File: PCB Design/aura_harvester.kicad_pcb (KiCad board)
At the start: 2 copper layers, 44.9 x 21.1 mm, 34 parts, among them J1 Conn_01x01_Pin, J2 Conn_01x01_Pin, J3 Conn_01x01_Pin, J4 Conn_01x01_Pin, J5 Conn_01x01_Pin, U1 ADG936BRUZ

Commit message: AURA PCB design
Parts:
- moved C11 70.6 mm to (64.2, 51.8), turned to 90 degrees
- moved L1 68.2 mm to (70.5, 49.6), turned to 180 degrees
- moved C8 62.0 mm to (69.0, 55.2), turned to -90 degrees
- moved C7 60.0 mm to (69.4, 61.8), turned to -90 degrees
- moved C3 55.0 mm to (72.5, 55.2), turned to -90 degrees
- moved C6 53.4 mm to (78.3, 55.1), turned to -90 degrees
- moved C1 52.5 mm to (72.2, 61.8), turned to -90 degrees
- moved R2 51.6 mm to (82.9, 63.8), turned to 180 degrees
- moved C2 51.5 mm to (75.2, 55.2), turned to -90 degrees
- moved C4 51.4 mm to (75.1, 61.7), turned to -90 degrees
- moved J1 50.3 mm to (64.2, 47.8)
- moved C5 49.5 mm to (78.2, 61.6), turned to -90 degrees
- moved C10 43.9 mm to (88.2, 60.6), turned to -90 degrees
- moved D1 43.7 mm to (68.2, 58.5), turned to -90 degrees
- moved D2 42.8 mm to (69.7, 58.5), turned to 90 degrees
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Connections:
- C10 pad 2: Net-(C10-Pad2) -> GND
- C9 pad 2: Net-(C10-Pad2) -> GND
- R2 pad 2: Net-(R2-Pad2) -> GND
- U1 pad 11: Net-(R2-Pad2) -> GND
- U1 pad 13: Net-(R2-Pad2) -> GND
- U1 pad 15: Net-(R2-Pad2) -> GND
- U1 pad 16: Net-(R2-Pad2) -> GND
- U1 pad 18: Net-(U1-GND-Pad18) -> GND
- U1 pad 20: Net-(U1-GND-Pad18) -> GND
- U1 pad 3: Net-(C10-Pad2) -> GND
- U1 pad 5: Net-(C10-Pad2) -> GND
- U1 pad 6: Net-(C10-Pad2) -> GND
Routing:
- net /CLK: track 0.00 -> 5.64 mm
- added copper zone on F.Cu, net +3V3
- added copper zone on F.Cu, net /M_IN
- added copper zone on F.Cu, net Net-(D1-A)
- added copper zone on F.Cu, net Net-(D3-A)
- added copper zone on F.Cu, net Net-(D5-A)
- added copper zone on F.Cu, net Net-(D8-A)
- added copper zone on F.Cu, net Net-(U1-RF2A)
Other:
- board size 44.9 x 21.1 mm -> 34.3 x 21.1 mm

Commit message: Completed Routing and Silkscreen
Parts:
- added G***: LOGO, Logos:Lions_logo, F.Cu at (60.0, 47.3)
- added G***: LOGO, logos:sra_logo_small_neg, F.Cu at (78.6, 51.5)
- Ambient Antenna: renamed from AE2
- Harvest Antenna: renamed from AE1
- L2: footprint Capacitor_SMD:C_0402_1005Metric_Pad0.74x0.62mm_HandSolder -> Inductor_SMD:L_0402_1005Metric_Pad0.77x0.64mm_HandSolder
- moved Ambient Antenna 0.95 mm to (62.4, 58.0)
- moved C11 0.73 mm to (64.9, 51.8)
- moved C15 0.72 mm to (67.9, 64.0)
- moved C1 0.50 mm to (72.7, 61.8)
- moved C2 0.50 mm to (75.7, 55.2)
- moved C3 0.50 mm to (73.0, 55.2)
- moved C4 0.50 mm to (75.6, 61.7)
- moved C5 0.50 mm to (78.7, 61.6)
- moved C6 0.50 mm to (78.8, 55.1)
- moved C7 0.50 mm to (69.9, 61.8)
- moved C8 0.50 mm to (69.5, 55.2)
- moved D1 0.50 mm to (68.7, 58.5)
- moved D2 0.50 mm to (70.2, 58.5)
- moved D3 0.50 mm to (71.8, 58.5)
- moved D4 0.50 mm to (73.3, 58.5)
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- renumbered J5 to 3V3, J3 to CLK
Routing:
- net /SMA_Sig: track 0.00 -> 5.59 mm
- net /Ambient_Source: track 0.00 -> 4.64 mm
- net Net-(D2-A): track 0.00 -> 4.15 mm
- net Net-(D6-A): track 0.00 -> 3.65 mm
- net Net-(D4-A): track 0.00 -> 3.41 mm
- net Net-(D1-K): track 0.00 -> 1.86 mm
- net GND: vias 0 -> 40
- added copper zone on F.Cu, net /Ambient_Source
- added copper zone on F.Cu, net /M_OUT
- added copper zone on B.Cu, net GND
- added copper zone on F.Cu, net GND
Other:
- board size 34.3 x 21.1 mm -> 33.8 x 20.5 mm
- board text added: "Soham Vhatkar Gaurav Patil Sarvaarth Narang Lakshya Lalwani Pushkar Dube"

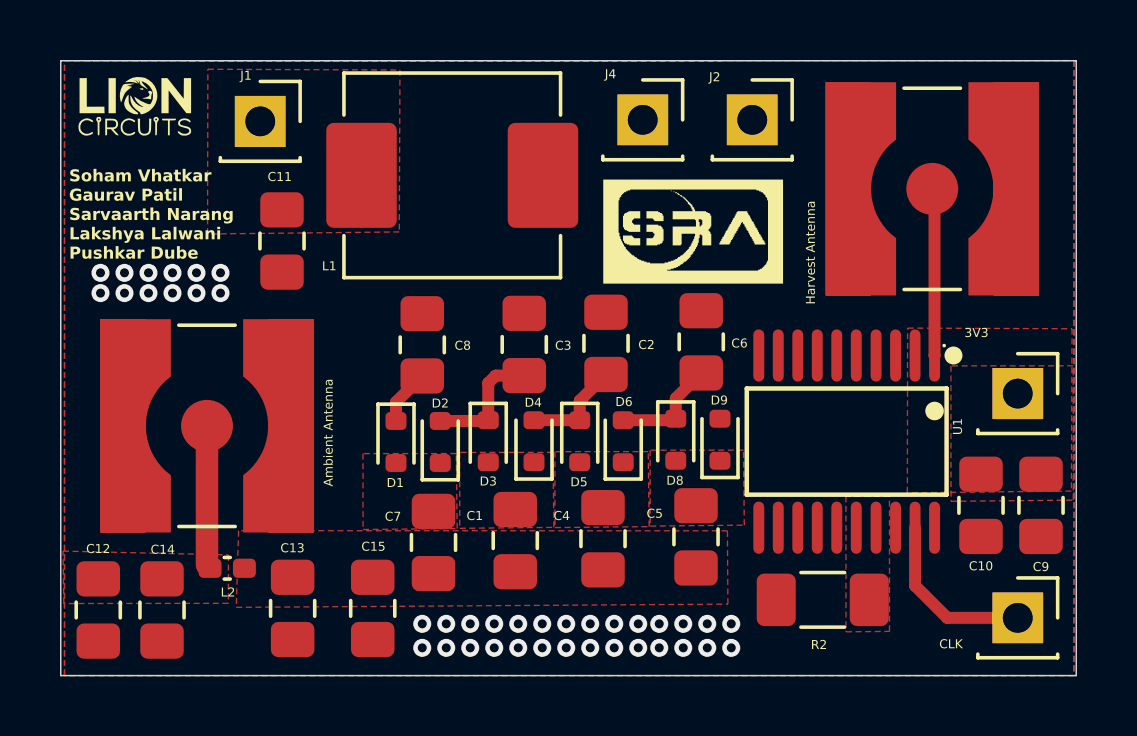
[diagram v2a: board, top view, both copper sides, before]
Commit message: Adding ground stitches and making the RF feed trace thick
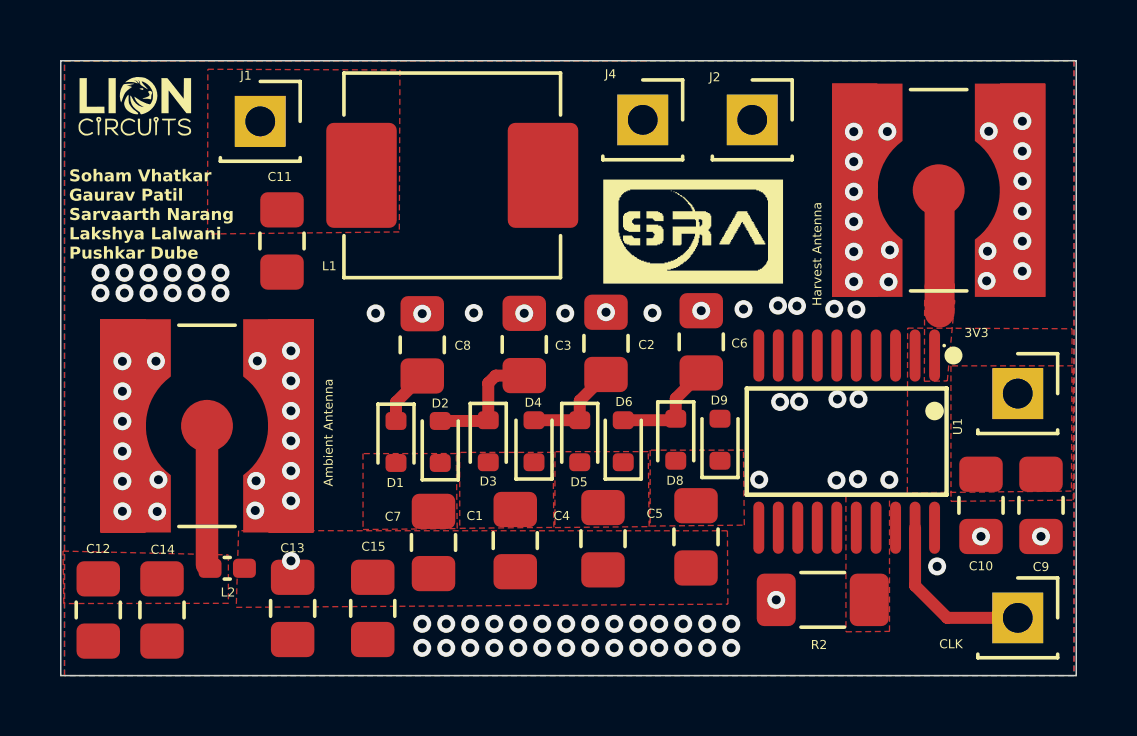
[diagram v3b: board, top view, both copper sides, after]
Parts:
- moved Harvest Antenna 0.22 mm to (86.8, 50.1)
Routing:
- net /SMA_Sig: track 5.59 -> 3.88 mm
- net GND: vias 40 -> 101
- net /M_IN: vias 0 -> 1
- added copper zone on F.Cu, net /SMA_Sig

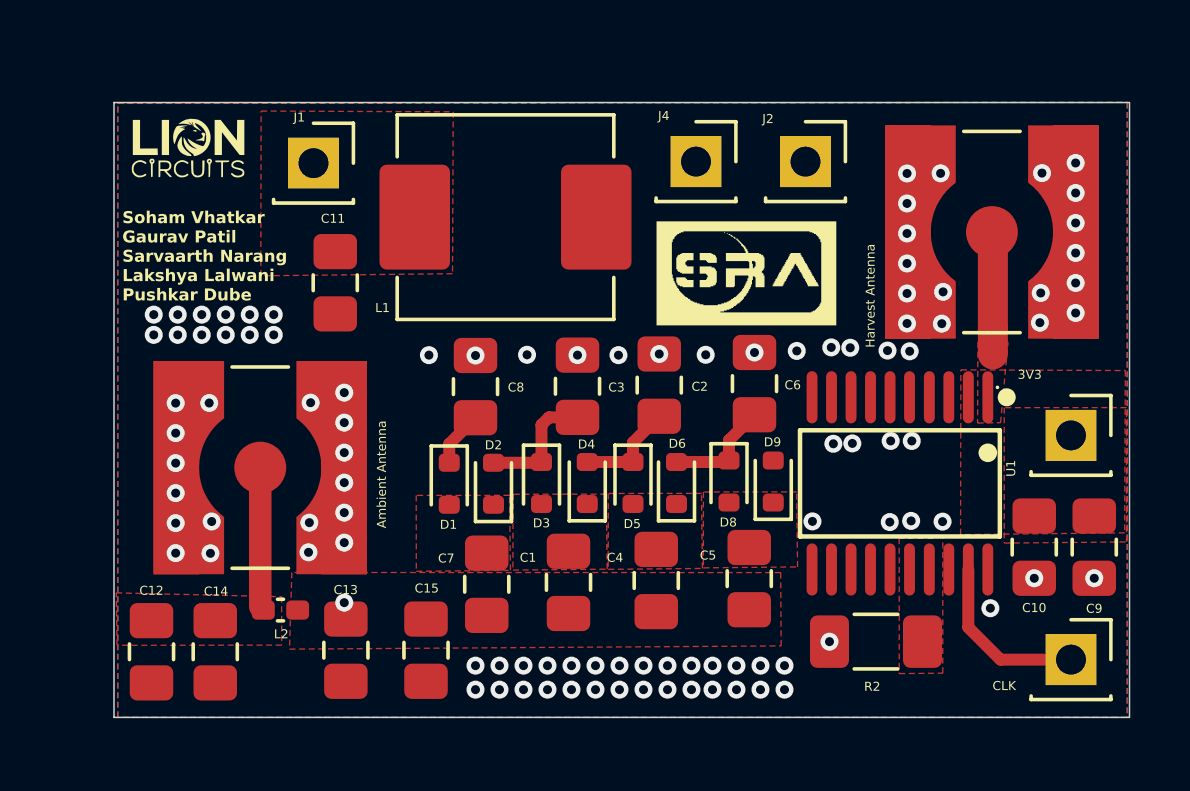
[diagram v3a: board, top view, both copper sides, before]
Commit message: modified SMA Antenna, RF diode Footprint, added testpoints
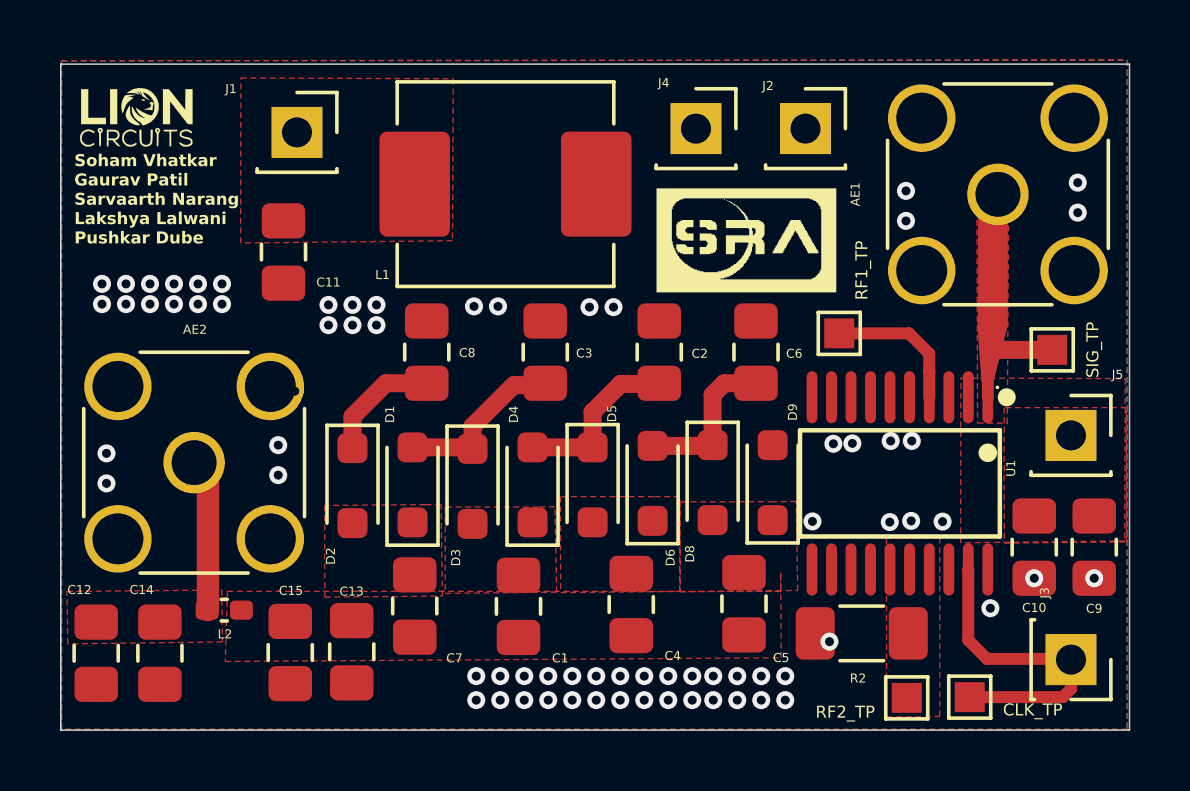
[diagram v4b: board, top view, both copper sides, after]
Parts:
- added CLK_TP: CLK_TP, TestPoint:TestPoint_Pad_1.0x1.0mm, F.Cu at (86.0, 65.6)
- added RF1_TP: RF1_TP, TestPoint:TestPoint_Pad_1.0x1.0mm, F.Cu at (81.7, 53.5)
- added RF2_TP: RF_TP, TestPoint:TestPoint_Pad_1.0x1.0mm, F.Cu at (83.9, 65.6)
- added SIG_TP: SIG_TP, TestPoint:TestPoint_Pad_1.0x1.0mm, F.Cu at (88.8, 54.0)
- AE1: renamed from Harvest Antenna; footprint Connector_Coaxial:SMA_Amphenol_132134-10_Vertical -> Connector_Coaxial:SMA_Amphenol_132134_Vertical
- AE2: renamed from Ambient Antenna; footprint Connector_Coaxial:SMA_Amphenol_132134-10_Vertical -> Connector_Coaxial:SMA_Amphenol_132134_Vertical
- D1, D2, D3, D4, D5, D6, D8, D9: footprint Diode_SMD:D_SOD-523 -> Diode_SMD:D_SOD-323_HandSoldering
- moved C15 4.53 mm to (63.4, 64.1)
- moved D1 3.23 mm to (65.5, 58.5)
- moved D2 2.70 mm to (67.5, 58.5)
- moved C7 2.51 mm to (67.5, 62.6)
- moved D3 2.30 mm to (69.5, 58.6)
- moved AE2 2.21 mm to (60.2, 57.8), turned to 180 degrees
- moved C11 2.01 mm to (63.1, 50.8)
- moved G*** 2.01 mm to (58.2, 46.3)
- moved C8 1.99 mm to (67.9, 54.1)
- moved L2 1.88 mm to (61.2, 62.7)
- moved C1 1.85 mm to (71.0, 62.6)
- moved C12 1.84 mm to (56.9, 64.1)
- moved C14 1.84 mm to (59.0, 64.1)
- moved D4 1.82 mm to (71.5, 58.5)
- moved C3 1.57 mm to (71.9, 54.1)
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- renumbered CLK to J3, 3V3 to J5
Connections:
- U1 pad 4: unconnected-(U1-RF1A-Pad4) -> Net-(U1-RF1A)
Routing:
- net Net-(U1-RF1A): track 0.00 -> 4.74 mm
- net /CLK: track 5.80 -> 10.5 mm
- net /SMA_Sig: track 3.88 -> 8.50 mm
- net Net-(D1-K): track 1.86 -> 4.26 mm
- net Net-(D4-A): track 3.41 -> 5.79 mm
- net Net-(D6-A): track 3.65 -> 5.29 mm
- net Net-(D2-A): track 4.15 -> 5.79 mm
- net GND: vias 101 -> 73
- net /M_IN: vias 1 -> 0
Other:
- board size 33.8 x 20.5 mm -> 35.6 x 22.2 mm
